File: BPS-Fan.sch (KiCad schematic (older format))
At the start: 21 parts, among them J1 LDRBRDConn, J2 FAN1, J3 FAN2, J4 FAN3, J5 FAN4, Q1 BUK9M34-100EX, Q2 BUK9M34-100EX, Q3 BUK9M34-100EX, Q4 BUK9M34-100EX

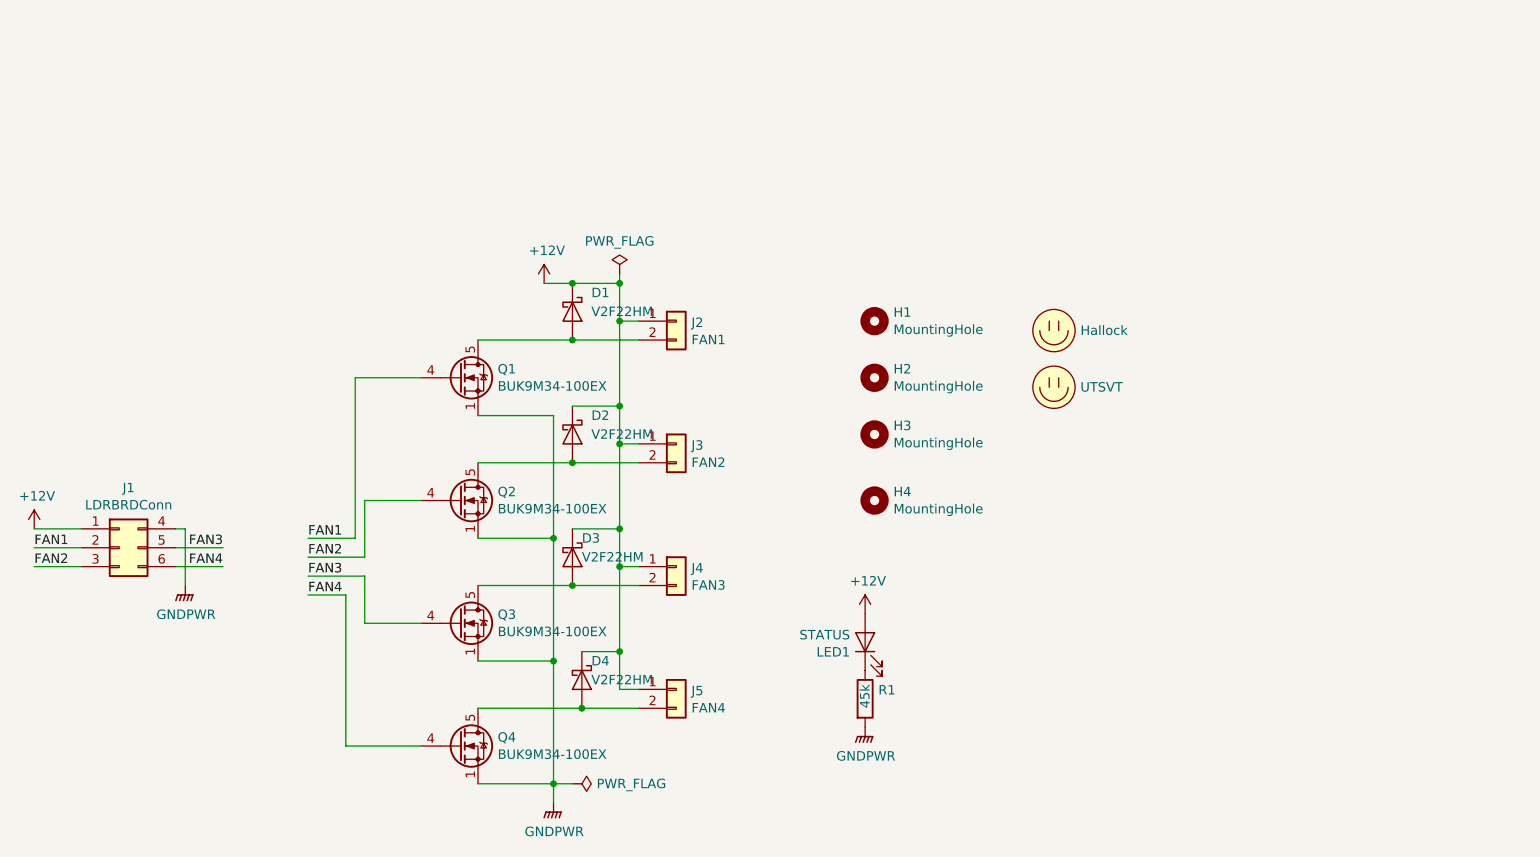
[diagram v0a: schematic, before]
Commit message: Adds pdf of schematic and PCB and png of PCB
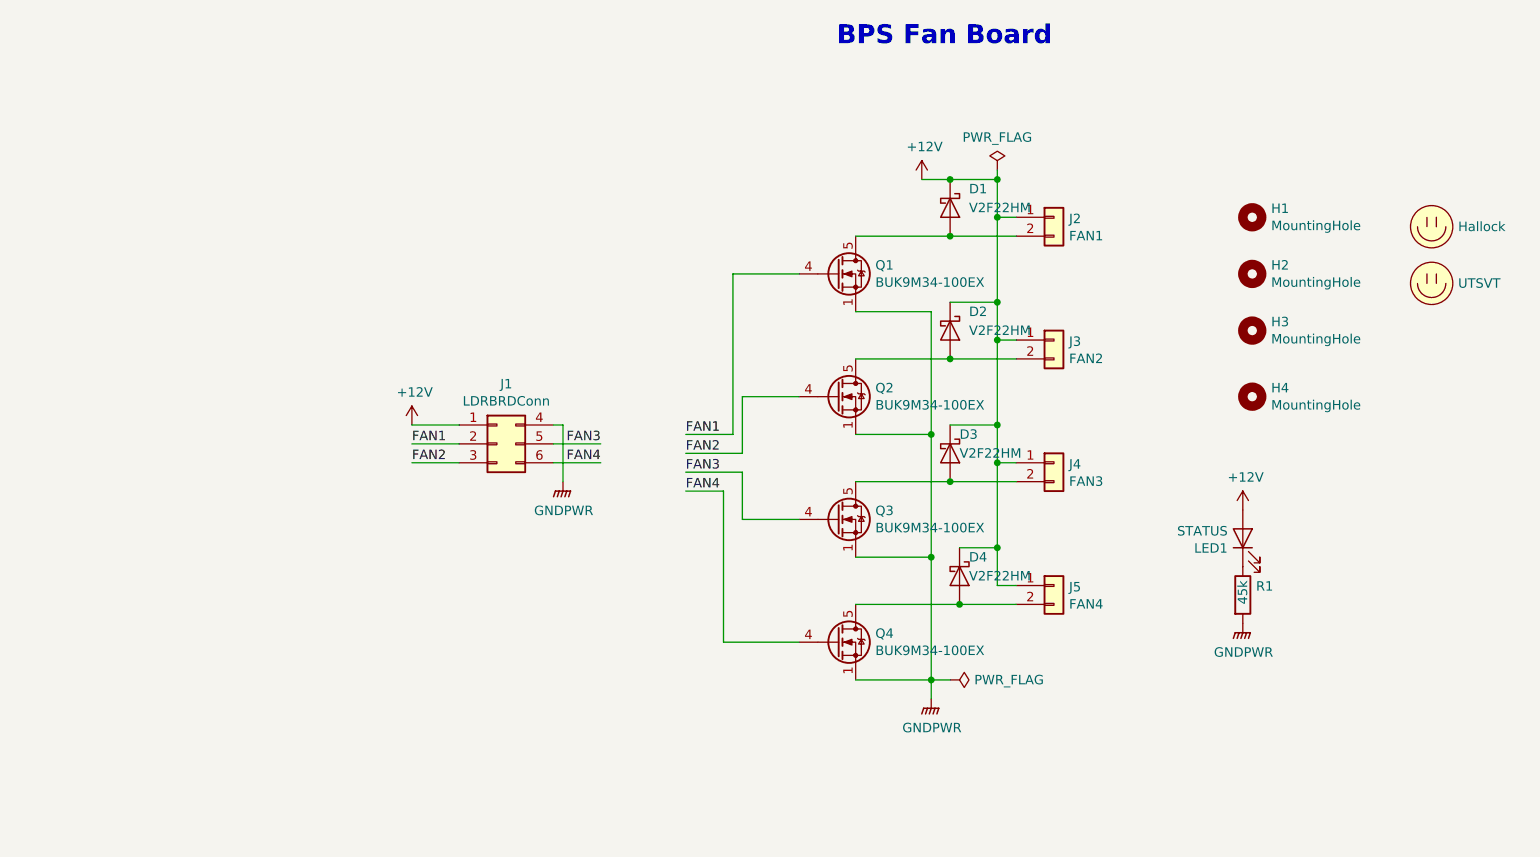
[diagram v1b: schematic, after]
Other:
- note added: "BPS Fan Board"
- moved on the sheet: D1, D2, D3, D4, H1, H2, H3, H4, J1, J2, J3, J4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
